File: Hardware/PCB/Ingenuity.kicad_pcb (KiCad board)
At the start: 4 copper layers, 65 x 30 mm, 38 parts, among them J1 Conn_ST_STDC14, J2 Conn_02x20_Odd_Even, J3 Conn_02x05_Odd_Even, J4 Conn_01x02, J5 Conn_01x02, J7 Conn_01x03, J8 Conn_01x03, J9 Conn_01x02, Q1 NMOS, Q2 NMOS, SW1 SW_SPDT, U1 STM32L412KBTx, U3 LSM6DSM, U4 AMS1117-3.3

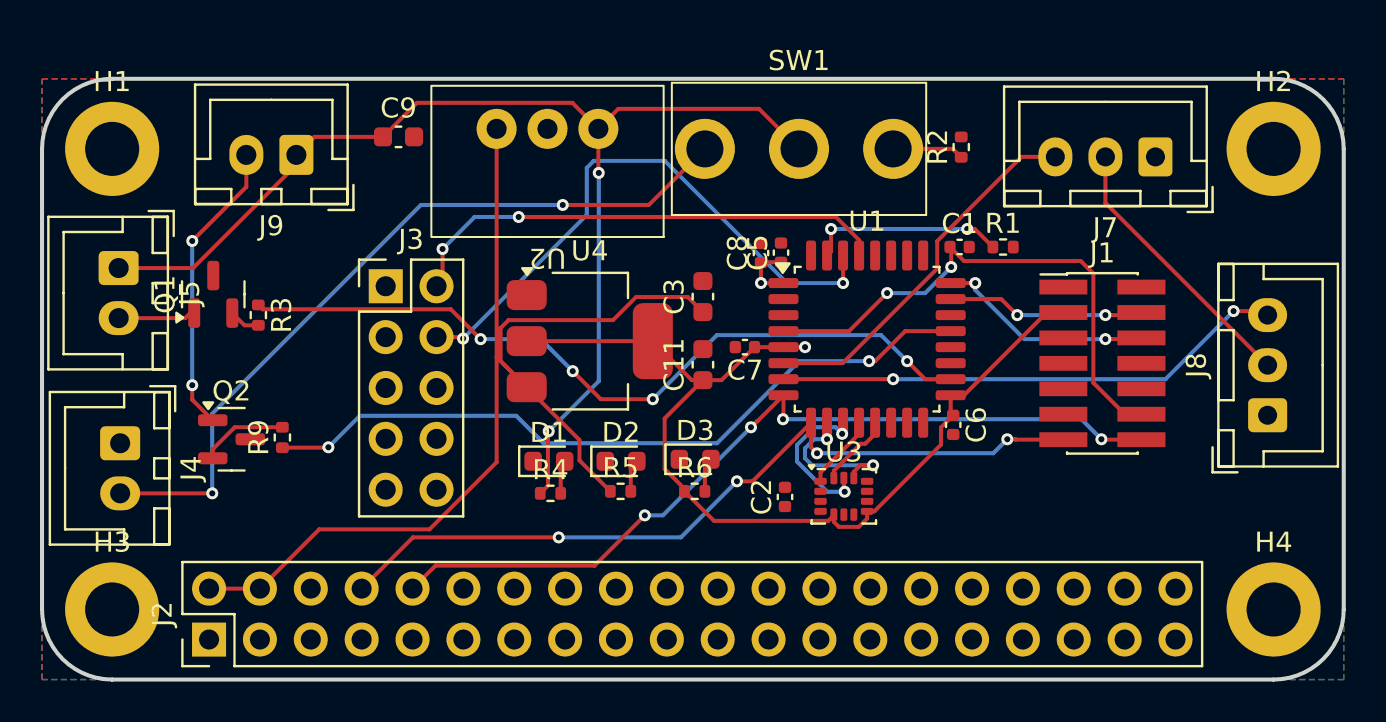
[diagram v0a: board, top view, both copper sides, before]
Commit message: update schematic, switch pins, change zones and routing
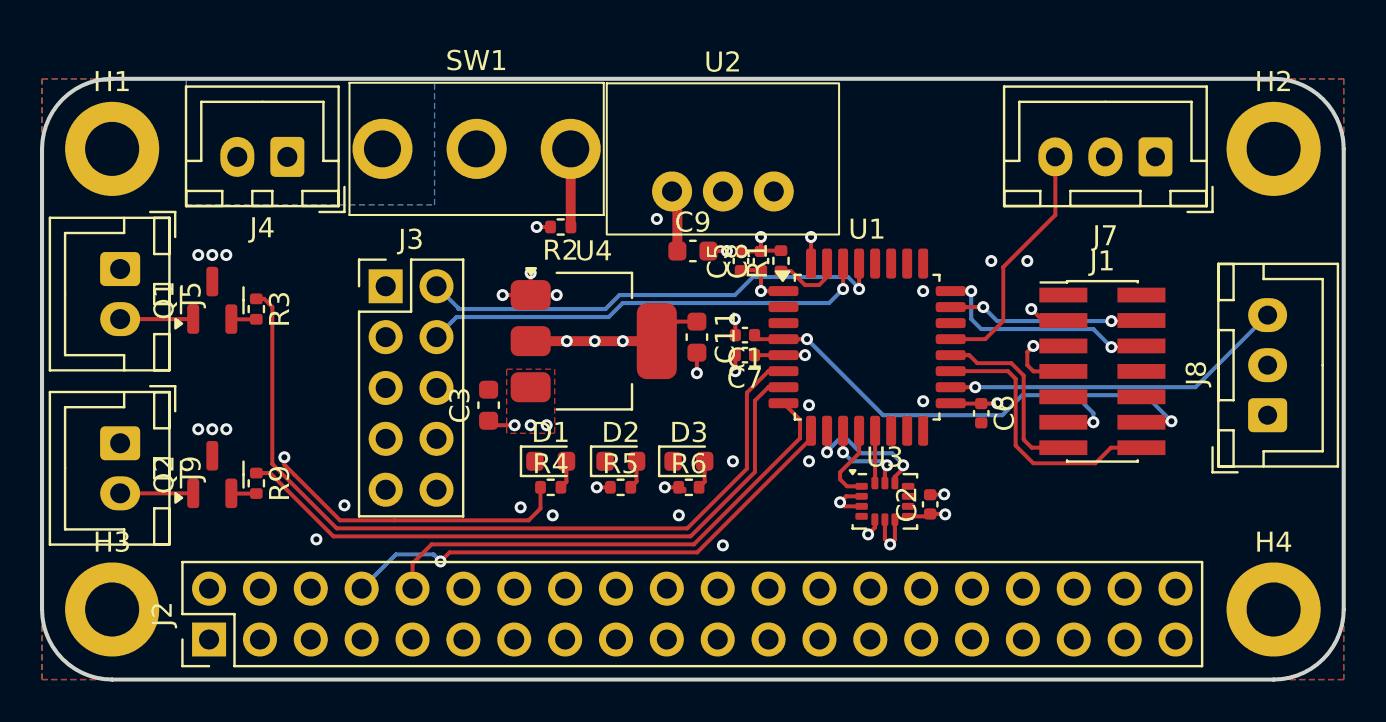
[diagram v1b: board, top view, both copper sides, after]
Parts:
- moved R2 20.4 mm to (171.9, 53.9), turned to 180 degrees
- moved J9 16.9 mm to (149.9, 64.7), turned to -90 degrees
- moved J4 16.6 mm to (158.2, 50.4), turned to 180 degrees
- moved SW1 16.1 mm to (167.7, 50.0)
- moved C9 15.8 mm to (178.5, 55.1)
- moved C3 12.0 mm to (168.3, 62.8)
- moved C1 11.6 mm to (181.1, 59.3), turned to 180 degrees
- moved R1 11.1 mm to (182.9, 55.6), turned to 90 degrees
- moved U2 9.30 mm to (180.0, 52.1), turned to 0 degrees
- moved C2 7.26 mm to (190.3, 67.8)
- moved R9 2.63 mm to (156.7, 66.7), turned to -90 degrees
- moved U3 2.07 mm to (188.1, 67.6)
- moved C5 2.04 mm to (180.9, 55.6)
- moved Q2 2.01 mm to (154.5, 66.3), turned to 90 degrees
- moved C6 1.52 mm to (192.9, 63.2)
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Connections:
- J1 pad 13: USART2_RX -> USART1_RX
- J1 pad 14: USART2_TX -> USART1_TX
- U1 pad 18: PWM1 -> PWM4
- U1 pad 21: PWM2 -> PWM3
- U1 pad 6: PWM3 -> PWM1
- U1 pad 7: PWM4 -> PWM2
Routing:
- net +5V: track 71.0 -> 2.47 mm, vias 0 -> 4
- net +7.5V: track 58.9 -> 20.2 mm, vias 2 -> 1
- net +BATT: track 38.7 -> 0.00 mm, vias 2 -> 0
- net +3.3V: track 51.4 -> 23.0 mm, vias 2 -> 10
- net GND: track 0.00 -> 25.0 mm, vias 0 -> 35
- net USART2_TX: track 42.1 -> 25.3 mm, vias 4 -> 0
- net USART2_RX: track 40.1 -> 26.2 mm, vias 4 -> 1
- net USART1_TX: track 0.00 -> 13.7 mm
- net Net-(J9-Pin_2): track 14.8 -> 3.65 mm, vias 2 -> 0
- net USART1_RX: track 0.00 -> 9.41 mm
- net PWM4: track 25.7 -> 17.3 mm, vias 2 -> 1
- net I2C1_SDA: track 29.3 -> 22.6 mm, vias 2 -> 1
- net Net-(U1-PH3): track 9.86 -> 3.43 mm, vias 2 -> 0
- net PWM3: track 18.6 -> 12.3 mm
- net PWM2: track 36.9 -> 32.8 mm, vias 2 -> 0
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- added copper zone on F.Cu, net +5V
- added copper zone on In1.Cu, net +5V
- added copper zone on In1.Cu, net +7.5V
- added copper zone on B.Cu, net +BATT

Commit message: add led, button
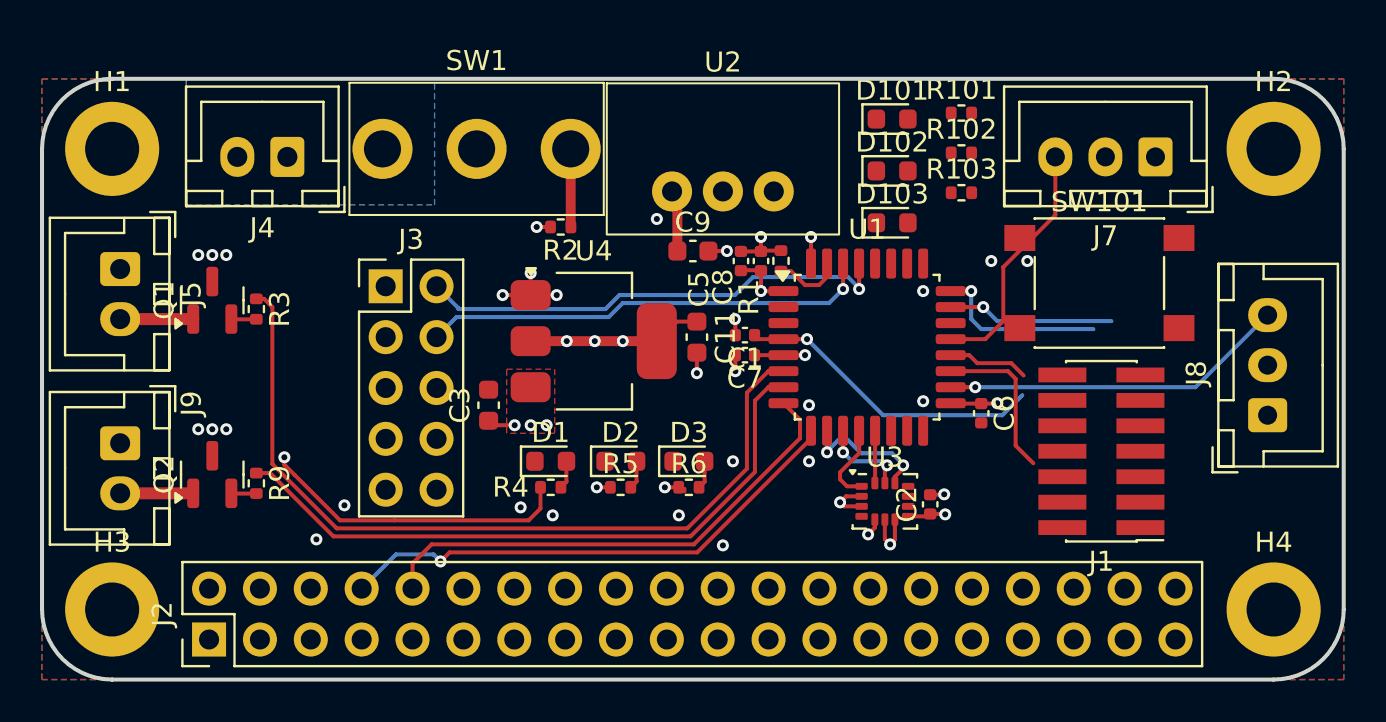
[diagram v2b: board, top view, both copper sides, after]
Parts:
- added D101: LED, LED_SMD:LED_0603_1608Metric, F.Cu at (188.4, 48.5)
- added D102: LED, LED_SMD:LED_0603_1608Metric, F.Cu at (188.4, 51.1)
- added D103: LED, LED_SMD:LED_0603_1608Metric, F.Cu at (188.4, 53.7)
- added R101: 165, Resistor_SMD:R_0402_1005Metric, F.Cu at (191.9, 48.2)
- added R102: 165, Resistor_SMD:R_0402_1005Metric, F.Cu at (191.9, 50.2)
- added R103: 165, Resistor_SMD:R_0402_1005Metric, F.Cu at (191.9, 52.2)
- added SW101: SW_Push, Button_Switch_SMD:SW_Push_1P1T_NO_6x6mm_H9.5mm, F.Cu at (198.8, 56.7)
- moved J1 3.99 mm to (198.9, 65.1), turned to 180 degrees
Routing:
- net NRST: track 25.0 -> 15.4 mm, vias 2 -> 1
- net GND: track 25.0 -> 17.9 mm, vias 35 -> 33
- net USART1_TX: track 13.7 -> 7.98 mm
- net USART1_RX: track 9.41 -> 4.06 mm
- net SWCLK: track 11.5 -> 8.73 mm, vias 2 -> 1
- net +3.3V: track 23.0 -> 20.3 mm, vias 10 -> 9
- net SWDIO: track 9.83 -> 8.31 mm, vias 2 -> 1
